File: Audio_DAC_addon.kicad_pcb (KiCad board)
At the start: 2 copper layers, 96.8 x 90.1 mm, 8 parts, among them J16 Conn_01x10, J17 Conn_01x08, J25 Conn_01x10, J28 Conn_01x10, J29 Conn_01x01

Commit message: real initial commit
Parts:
- added C10: 1uF, Capacitors_SMD:C_0402_NoSilk, F.Cu at (83.8, 94.9)
- added C4: 1uF, Capacitors_SMD:C_0402_NoSilk, F.Cu at (89.1, 96.1)
- added C5: 1uF, Capacitors_SMD:C_0402_NoSilk, F.Cu at (90.8, 95.0)
- added C6: 2.2uF, Capacitors_SMD:C_0402_NoSilk, F.Cu at (83.8, 94.0)
- added C7: 1uF, Capacitors_SMD:C_0402_NoSilk, F.Cu at (83.8, 93.1)
- added C8: 1uF, Capacitors_SMD:C_0402_NoSilk, F.Cu at (83.8, 92.3)
- added C9: 1uF, Capacitors_SMD:C_0402_NoSilk, F.Cu at (83.8, 91.4)
- added J1: Audio-Jack-3, custom:AUB-11_audio-jack, F.Cu at (66.4, 91.0)
- added R1: R, Resistors_SMD:R_0603_HandSoldering, F.Cu at (88.0, 98.4)
- added R2: R, Resistors_SMD:R_0603_HandSoldering, F.Cu at (86.4, 98.4)
- added R3: R, Resistors_SMD:R_0603_HandSoldering, F.Cu at (90.2, 89.1)
- added U1: MAX9860, Housings_DFN_QFN:QFN-24-1EP_4x4mm_Pitch0.5mm, F.Cu at (87.6, 93.0)
- moved C3 9.20 mm to (82.8, 88.9)
- moved C1 7.97 mm to (82.8, 89.9)
- moved C2 7.91 mm to (82.7, 87.8)
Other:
- board size 96.8 x 90.1 mm -> 39.9 x 29.9 mm

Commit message: add LDOs + pcb progress
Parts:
- added C11: 1uF, Capacitors_SMD:C_0402_NoSilk, F.Cu at (79.8, 84.5)
- added C12: 1uF, Capacitors_SMD:C_0402_NoSilk, F.Cu at (79.0, 87.2)
- added C13: 1uF, Capacitors_SMD:C_0402_NoSilk, F.Cu at (79.0, 88.8)
- added C14: 1uF, Capacitors_SMD:C_0402_NoSilk, F.Cu at (77.5, 85.7)
- added C15: 1uF, Capacitors_SMD:C_0402_NoSilk, F.Cu at (76.2, 84.3)
- added C16: 1uF, Capacitors_SMD:C_0402_NoSilk, F.Cu at (80.2, 90.7)
- added R4: R, Resistors_SMD:R_0603_HandSoldering, F.Cu at (83.0, 94.1)
- added U2: TLV70033DCKR, TO_SOT_Packages_SMD:SOT-23-5, F.Cu at (82.2, 87.2)
- added U3: TLV70018DDCR, TO_SOT_Packages_SMD:SOT-23-5, F.Cu at (89.8, 87.0)
- added U4: TLV70018DDCR, TO_SOT_Packages_SMD:SOT-23-5, F.Cu at (74.5, 87.7)
- U1: moved to B.Cu
- moved C2 17.2 mm to (68.6, 77.9)
- moved C1 17.2 mm to (68.7, 80.0)
- moved C3 17.2 mm to (68.7, 79.0)
- moved R3 14.3 mm to (89.0, 103.3)
- moved C9 10.5 mm to (83.8, 101.9), turned to 0 degrees
- moved C8 8.77 mm to (83.8, 101.0), turned to 0 degrees
- moved U1 7.33 mm to (85.4, 100.0)
- moved C7 7.08 mm to (83.8, 100.1), turned to 0 degrees
- moved J1 7.04 mm to (66.4, 98.0)
- moved C5 5.22 mm to (87.3, 98.8), turned to 180 degrees
- moved C6 5.09 mm to (83.8, 99.1), turned to 0 degrees
- moved R2 4.52 mm to (84.8, 94.1), turned to 270 degrees
- moved R1 4.44 mm to (86.7, 94.1), turned to 270 degrees
- moved C4 3.85 mm to (85.8, 98.1), turned to 270 degrees
- moved C10 3.30 mm to (83.8, 98.2), turned to 0 degrees
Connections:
- net Net-(C10-Pad1) renamed /AVDD
- net Net-(R3-Pad2) renamed /IRQ
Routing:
- net GND: track 0.00 -> 0.86 mm, vias 0 -> 1

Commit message: pcb and circuit diagram are almost done
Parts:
- removed C1, C2, C3: 0.1, Capacitors_SMD:C_0402_NoSilk
- removed J17: Conn_01x08, Pin_Headers:Pin_Header_Straight_1x08_Pitch2.54mm
- removed J29: Conn_01x01, Mounting_Holes:MountingHole_3.2mm_M3_ISO7380_Pad
- added J2: Conn_01x03, Pin_Headers:Pin_Header_Straight_1x03_Pitch2.54mm, F.Cu at (72.3, 79.0)
- added R10: R, Resistors_SMD:R_0603_HandSoldering, F.Cu at (95.1, 85.7)
- added R11: R, Resistors_SMD:R_0603_HandSoldering, F.Cu at (102.3, 79.8)
- added R5: R, Resistors_SMD:R_0603_HandSoldering, F.Cu at (82.0, 80.8)
- added R6: R, Resistors_SMD:R_0603_HandSoldering, F.Cu at (83.7, 80.8)
- added R7: R, Resistors_SMD:R_0603_HandSoldering, F.Cu at (88.7, 80.8)
- added R8: R, Resistors_SMD:R_0603_HandSoldering, F.Cu at (90.7, 80.8)
- added R9: R, Resistors_SMD:R_0603_HandSoldering, F.Cu at (92.7, 80.8)
- moved C15 8.91 mm to (83.5, 89.4), turned to 180 degrees
- moved C16 8.88 mm to (71.3, 89.5)
- moved C12 6.82 mm to (85.8, 86.7), turned to 270 degrees
- moved C13 6.75 mm to (72.5, 86.7), turned to 270 degrees
- moved U3 6.60 mm to (83.2, 87.2), turned to 270 degrees
- moved U2 5.65 mm to (76.5, 87.2), turned to 270 degrees
- moved U4 4.62 mm to (69.9, 87.2), turned to 270 degrees
- moved C14 3.83 mm to (78.0, 89.5)
- moved C11 2.22 mm to (79.2, 86.7), turned to 270 degrees
- moved C7 0.90 mm to (83.0, 100.1)
- moved C6 0.60 mm to (83.2, 99.1)
- moved C8 0.60 mm to (83.2, 101.0)
- moved C5 0.51 mm to (87.2, 99.3), turned to 270 degrees
- moved R1 0.50 mm to (86.7, 93.6), turned to 90 degrees
- moved R2 0.50 mm to (84.8, 93.6)
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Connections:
- net Net-(J1-Pad1) renamed /OUTP
- net Net-(R2-Pad2) renamed /SDA
- net Net-(R4-Pad1) renamed /OUTN
- C12 pad 1: /DVDDIO_3V3 -> VCC
- C13 pad 1: /DVDDIO_3V3 -> VCC
- R1 pad 1: /DVDDIO_3V3 -> /SCL
- R1 pad 2: Net-(R1-Pad2) -> /DVDDIO_3V3
- U1 pad 10: Net-(R1-Pad2) -> /SCL
- U3 pad 1: /DVDDIO_3V3 -> VCC
- U3 pad 3: /DVDDIO_3V3 -> VCC
- U4 pad 1: /DVDDIO_3V3 -> VCC
- U4 pad 3: /DVDDIO_3V3 -> VCC
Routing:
- net /DVDDIO_3V3: track 0.00 -> 38.1 mm, vias 0 -> 4
- net GND: track 0.86 -> 25.0 mm, vias 1 -> 16
- net /LRCLK: track 0.00 -> 23.0 mm, vias 0 -> 1
- net /OUTP: track 0.00 -> 21.7 mm
- net /BCLK: track 0.00 -> 20.9 mm, vias 0 -> 1
- net /SDIN: track 0.00 -> 20.8 mm, vias 0 -> 1
- net /SCL: track 0.00 -> 18.9 mm, vias 0 -> 1
- net /AVDD: track 0.00 -> 18.7 mm, vias 0 -> 1
- net /SDA: track 0.00 -> 18.6 mm, vias 0 -> 1
- net /MCLK: track 0.00 -> 18.5 mm, vias 0 -> 1
- net /DVDD: track 0.00 -> 16.6 mm, vias 0 -> 4
- net /FPGA_AG11: track 0.00 -> 14.0 mm
- net /FPGA_AH9: track 0.00 -> 12.3 mm, vias 0 -> 1
- net Net-(J16-Pad9): track 0.00 -> 10.3 mm
- net VCC: track 0.00 -> 8.26 mm, vias 0 -> 6
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- added copper zone on B.Cu, net VCC
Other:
- outline, holes or cut-outs redrawn
- net class Default: clearance 0.18 -> 0.2
- rule trace_clearance: 0.18 -> 0.2
- board text added: "SDA"

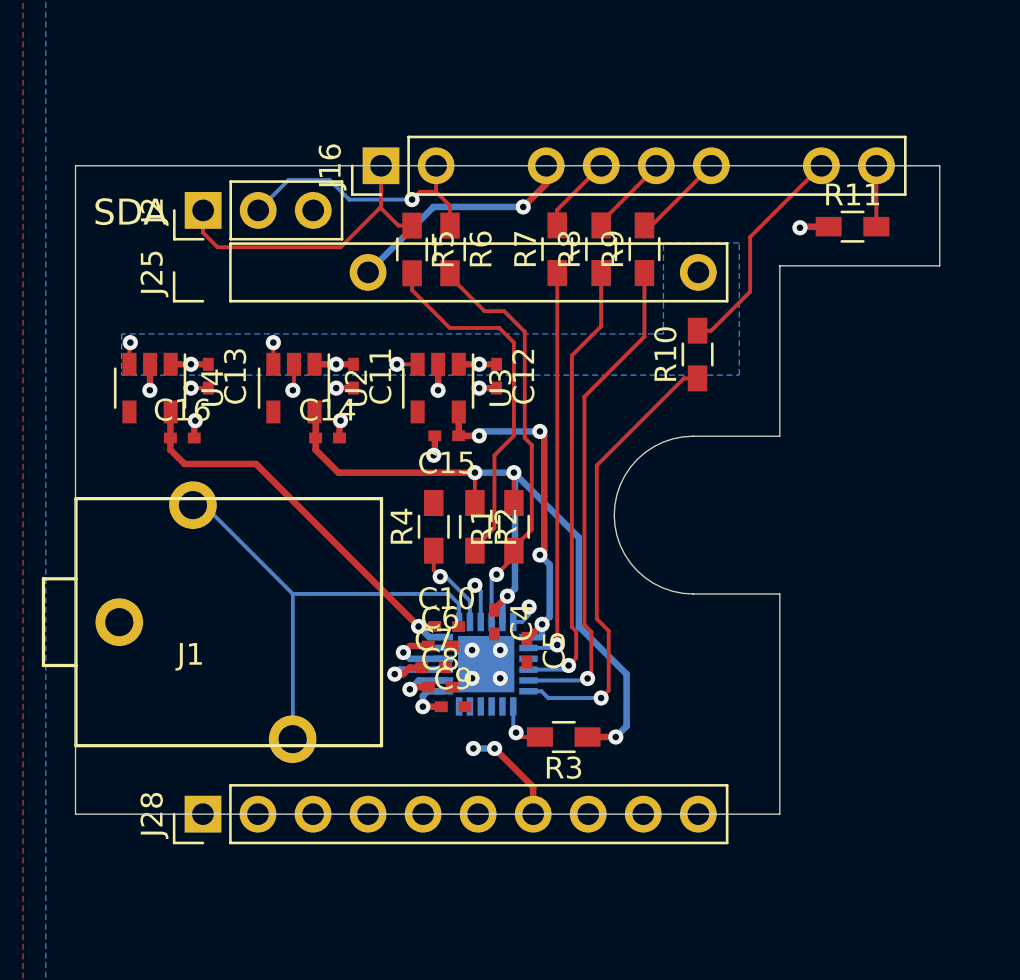
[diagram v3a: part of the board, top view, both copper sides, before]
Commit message: add silkscreen
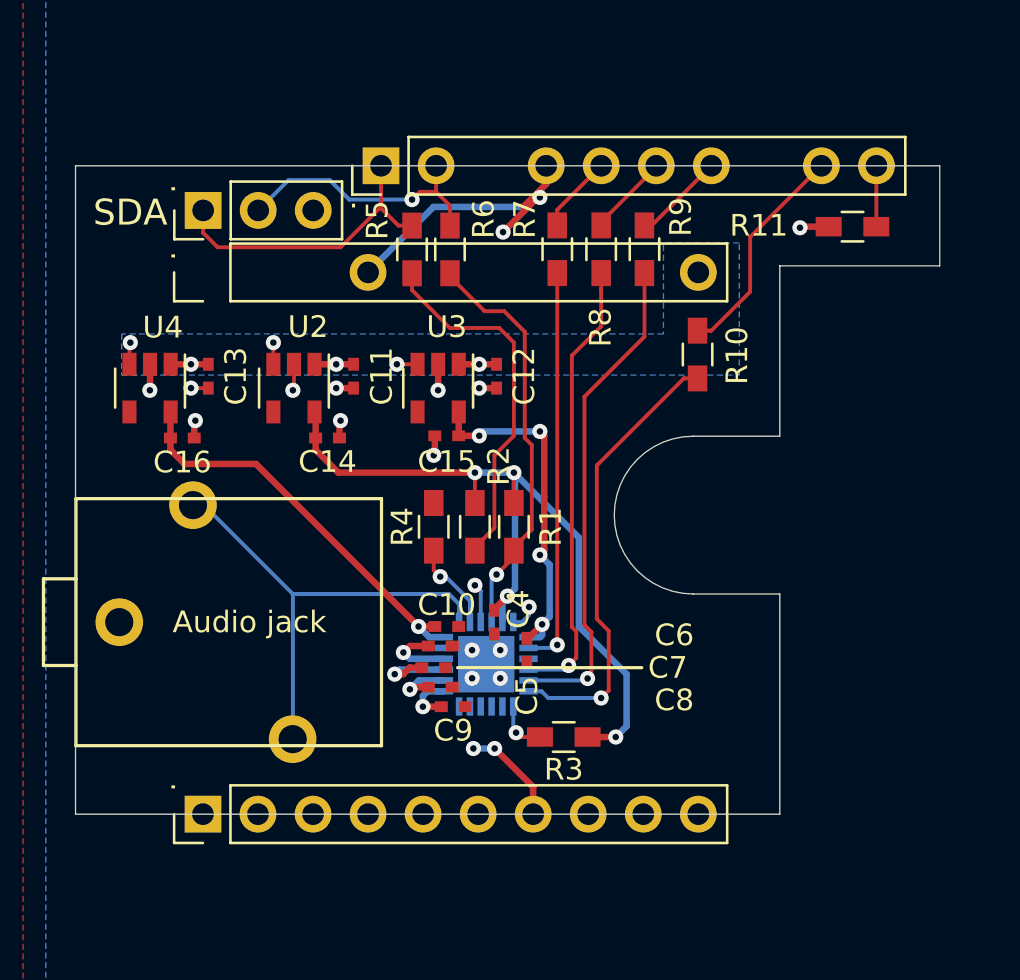
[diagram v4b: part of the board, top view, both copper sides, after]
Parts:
- Audio jack: renamed from J1
- renumbered J25 to ., J16 to ., J28 to ., J2 to .
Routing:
- net (no net): track 0.00 -> 2.36 mm, vias 1 -> 3
- net GND: vias 16 -> 15

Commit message: generate gerber + lots of bug fix
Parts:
- J1: renamed from Audio jack
- renumbered . to J16, . to J2, . to J25, . to J28
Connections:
- net Net-(C6-Pad1) renamed /REF
- net Net-(C7-Pad1) renamed /PREG
- net Net-(C8-Pad1) renamed /REG
- net Net-(C9-Pad1) renamed /MICBIAS
- net Net-(J16-Pad10) renamed /FPGA_AF17
- net Net-(J16-Pad9) renamed /FPGA_AE15
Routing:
- net GND: track 25.0 -> 125.3 mm, vias 15 -> 50
- net (no net): track 2.36 -> 0.00 mm, vias 3 -> 0
- net /SDA: track 18.6 -> 20.2 mm
- net /AVDD: track 18.7 -> 19.6 mm
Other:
- net class Default: clearance 0.2 -> 0.18
- rule trace_clearance: 0.2 -> 0.18
